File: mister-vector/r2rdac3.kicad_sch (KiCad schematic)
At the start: 6 parts

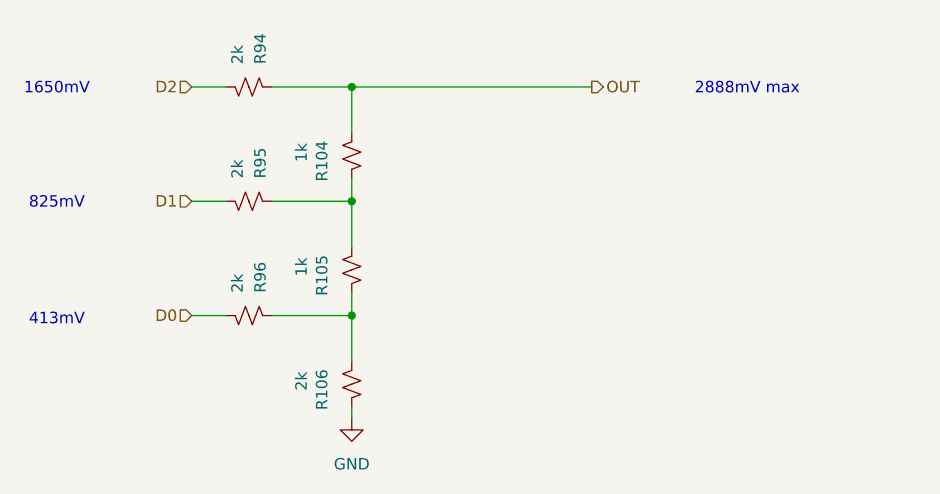
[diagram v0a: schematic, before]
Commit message: hierarchical schematic, add libraries
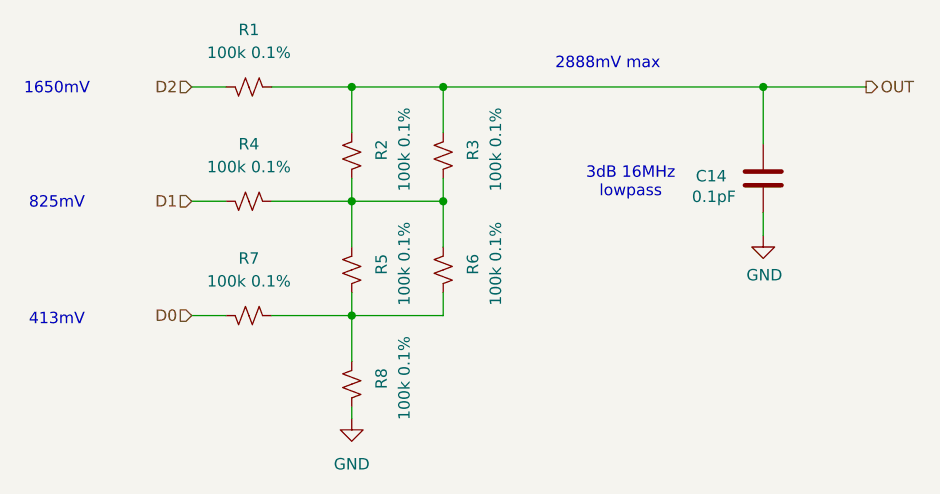
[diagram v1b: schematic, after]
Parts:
- added C14: 0.1pF, Capacitor_SMD:C_0402_1005Metric, symbol Device:C
- added R3, R6: 100k 0.1%, Resistor_SMD:R_0402_1005Metric, symbol Device:R_Small_US
- R1: renamed from R94; value 2k -> 100k 0.1%; LCSC (none) -> C852472
- R2: renamed from R104; value 1k -> 100k 0.1%; LCSC (none) -> C852472
- R4: renamed from R95; value 2k -> 100k 0.1%; LCSC (none) -> C852472
- R5: renamed from R105; value 1k -> 100k 0.1%; LCSC (none) -> C852472
- R7: renamed from R96; value 2k -> 100k 0.1%; LCSC (none) -> C852472
- R8: renamed from R106; value 2k -> 100k 0.1%; LCSC (none) -> C852472
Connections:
- net GND: now also C14.1
- net OUT: now also C14.2, R3.1
- net at R5.2, R7.1, R8.1: now also R6.2
- net at R2.2, R4.1, R5.1: now also R3.2, R6.1
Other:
- note added: "3dB 16MHz lowpass"
